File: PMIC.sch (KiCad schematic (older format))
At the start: 71 parts, among them U4 CSD86330Q3D, U5 LMR62014XMF_NOPB, U6 CSD86330Q3D, U8 TPS65086100

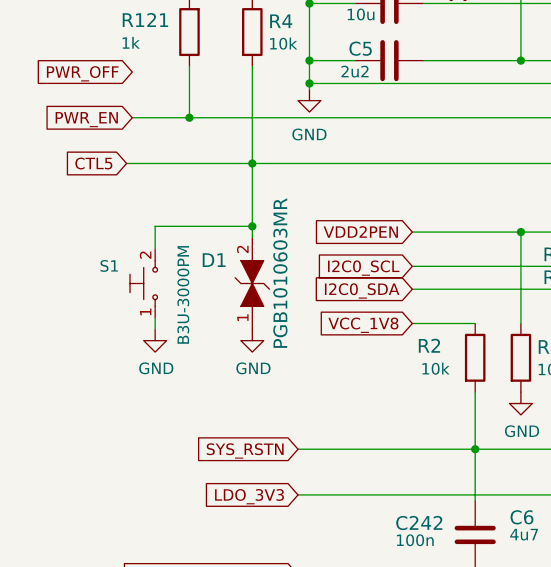
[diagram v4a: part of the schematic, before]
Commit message: Layout: 5v8 dcdc, clocks, SPIFlash, testpoints
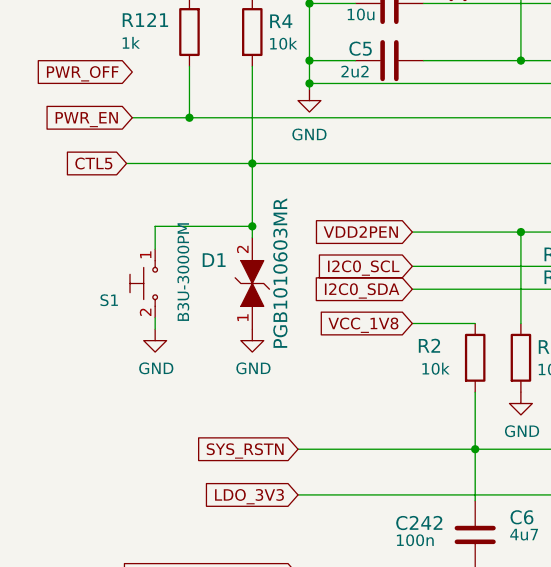
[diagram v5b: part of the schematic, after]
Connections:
- net CTL5: now also S1.1; no longer S1.2
- net GND: now also S1.2; no longer S1.1
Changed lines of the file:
@@
 5V8 boost regulator
-$Comp
-L arvsom:B3U-3000PM S1
-U 1 1 608A76FB
-P 3500 4850
-F 0 "S1" V 3575 5050 50  0000 C CNN
-F 1 "B3U-3000PM" H 3450 4725 50  0000 C CNN
-F 2 "arvsom-footprints:B3U-3000P" H 3700 5050 50  0001 L CNN
-F 3 "http://www.farnell.com/datasheets/2610940.pdf" H 3700 5150 60  0001 L CNN
-F 4 "B3U-3000PM" H 3696 5243 60  0001 L CNN "MPN"
-F 5 "OMRON" H 3700 5322 60  0001 L CNN "Manufacturer"
-	1    3500 4850
-	0    -1   -1   0
-$EndComp
 $Comp
 L arvsom:CSD86330Q3D U4
@@
 	1    0    0    -1
 $EndComp
+$Comp
+L arvsom:B3U-3000PM S1
+U 1 1 608A76FB
+P 3500 4850
+F 0 "S1" V 3575 5050 50  0000 C CNN
+F 1 "B3U-3000PM" H 3450 4725 50  0000 C CNN
+F 2 "arvsom-footprints:B3U-3000P" H 3700 5050 50  0001 L CNN
+F 3 "http://www.farnell.com/datasheets/2610940.pdf" H 3700 5150 60  0001 L CNN
+F 4 "B3U-3000PM" H 3696 5243 60  0001 L CNN "MPN"
+F 5 "OMRON" H 3700 5322 60  0001 L CNN "Manufacturer"
+	1    3500 4850
+	0    -1   1    0
+$EndComp
 $EndSCHEMATC

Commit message: Update libs
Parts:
- R10, R11, R12, R123, R14, R15, R16, R5, R6: footprint antmicro-footprints:0201-res -> arvsom-footprints:0201-res; symbol antmicroResistorsmisc:R_0R_0201 -> arvsom:R_0R_0201
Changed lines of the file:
@@
 	4625 4775 5275 4775
 $Comp
-L antmicroResistorsmisc:R_0R_0201 R5
+L arvsom:R_0R_0201 R5
 U 1 1 60A1EF73
 P 5425 4775
 F 0 "R5" H 5250 4825 60  0000 C CNN
 F 1 "R_0R_0201" H 5425 4625 60  0001 C CNN
-F 2 "antmicro-footprints:0201-res" H 5625 4975 60  0001 L CNN
+F 2 "arvsom-footprints:0201-res" H 5625 4975 60  0001 L CNN
 F 3 "" H 5425 4775 50  0001 C CNN
 F 4 "VISHAY" H 5625 5175 60  0001 L CNN "Manufacturer"
@@
 $EndComp
 $Comp
-L antmicroResistorsmisc:R_0R_0201 R6
+L arvsom:R_0R_0201 R6
 U 1 1 60A26BB5
 P 5425 4875
 F 0 "R6" H 5250 4925 60  0000 C CNN
 F 1 "R_0R_0201" H 5425 4725 60  0001 C CNN
-F 2 "antmicro-footprints:0201-res" H 5625 5075 60  0001 L CNN
+F 2 "arvsom-footprints:0201-res" H 5625 5075 60  0001 L CNN
 F 3 "" H 5425 4875 50  0001 C CNN
 F 4 "VISHAY" H 5625 5275 60  0001 L CNN "Manufacturer"
@@
 $EndComp
 $Comp
-L antmicroResistorsmisc:R_0R_0201 R123
+L arvsom:R_0R_0201 R123
 U 1 1 60A2A03C
 P 5425 5575
 F 0 "R123" H 5375 5675 60  0000 C CNN
 F 1 "R_0R_0201" H 5425 5425 60  0001 C CNN
-F 2 "antmicro-footprints:0201-res" H 5625 5775 60  0001 L CNN
+F 2 "arvsom-footprints:0201-res" H 5625 5775 60  0001 L CNN
 F 3 "" H 5425 5575 50  0001 C CNN
 F 4 "VISHAY" H 5625 5975 60  0001 L CNN "Manufacturer"
@@
 $EndComp
 $Comp
-L antmicroResistorsmisc:R_0R_0201 R10
+L arvsom:R_0R_0201 R10
 U 1 1 60A468A9
 P 8500 3775
 F 0 "R10" H 8275 3825 60  0000 C CNN
 F 1 "R_0R_0201" H 8500 3625 60  0001 C CNN
-F 2 "antmicro-footprints:0201-res" H 8700 3975 60  0001 L CNN
+F 2 "arvsom-footprints:0201-res" H 8700 3975 60  0001 L CNN
 F 3 "" H 8500 3775 50  0001 C CNN
 F 4 "VISHAY" H 8700 4175 60  0001 L CNN "Manufacturer"
@@
 $EndComp
 $Comp
-L antmicroResistorsmisc:R_0R_0201 R11
+L arvsom:R_0R_0201 R11
 U 1 1 60A4B370
 P 8500 3875
 F 0 "R11" H 8275 3925 60  0000 C CNN
 F 1 "R_0R_0201" H 8500 3725 60  0001 C CNN
-F 2 "antmicro-footprints:0201-res" H 8700 4075 60  0001 L CNN
+F 2 "arvsom-footprints:0201-res" H 8700 4075 60  0001 L CNN
 F 3 "" H 8500 3875 50  0001 C CNN
 F 4 "VISHAY" H 8700 4275 60  0001 L CNN "Manufacturer"
@@
 $EndComp
 $Comp
-L antmicroResistorsmisc:R_0R_0201 R12
+L arvsom:R_0R_0201 R12
 U 1 1 60A4C09F
 P 8500 4075
 F 0 "R12" H 8275 4125 60  0000 C CNN
 F 1 "R_0R_0201" H 8500 3925 60  0001 C CNN
-F 2 "antmicro-footprints:0201-res" H 8700 4275 60  0001 L CNN
+F 2 "arvsom-footprints:0201-res" H 8700 4275 60  0001 L CNN
 F 3 "" H 8500 4075 50  0001 C CNN
 F 4 "VISHAY" H 8700 4475 60  0001 L CNN "Manufacturer"
@@
 $EndComp
 $Comp
-L antmicroResistorsmisc:R_0R_0201 R14
+L arvsom:R_0R_0201 R14
 U 1 1 60A523FE
 P 8500 5375
 F 0 "R14" H 8275 5425 60  0000 C CNN
 F 1 "R_0R_0201" H 8500 5225 60  0001 C CNN
-F 2 "antmicro-footprints:0201-res" H 8700 5575 60  0001 L CNN
+F 2 "arvsom-footprints:0201-res" H 8700 5575 60  0001 L CNN
 F 3 "" H 8500 5375 50  0001 C CNN
 F 4 "VISHAY" H 8700 5775 60  0001 L CNN "Manufacturer"
@@
 $EndComp
 $Comp
-L antmicroResistorsmisc:R_0R_0201 R15
+L arvsom:R_0R_0201 R15
 U 1 1 60A56682
 P 8500 5475
 F 0 "R15" H 8275 5525 60  0000 C CNN
 F 1 "R_0R_0201" H 8500 5325 60  0001 C CNN
-F 2 "antmicro-footprints:0201-res" H 8700 5675 60  0001 L CNN
+F 2 "arvsom-footprints:0201-res" H 8700 5675 60  0001 L CNN
 F 3 "" H 8500 5475 50  0001 C CNN
 F 4 "VISHAY" H 8700 5875 60  0001 L CNN "Manufacturer"
@@
 $EndComp
 $Comp
-L antmicroResistorsmisc:R_0R_0201 R16
+L arvsom:R_0R_0201 R16
 U 1 1 60A57367
 P 8500 5675
 F 0 "R16" H 8275 5725 60  0000 C CNN
 F 1 "R_0R_0201" H 8500 5525 60  0001 C CNN
-F 2 "antmicro-footprints:0201-res" H 8700 5875 60  0001 L CNN
+F 2 "arvsom-footprints:0201-res" H 8700 5875 60  0001 L CNN
 F 3 "" H 8500 5675 50  0001 C CNN
 F 4 "VISHAY" H 8700 6075 60  0001 L CNN "Manufacturer"

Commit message: Update lib attributes
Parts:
- U2: renamed from U8; MPN (none) -> TPS65086100; Manufacturer (none) -> Texas Instruments
- U5: Manufacturer (none) -> Texas Instruments
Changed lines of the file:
@@
 $EndComp
 $Comp
-L arvsom:TPS65086100 U8
+L arvsom:TPS65086100 U2
 U 1 1 606F10CB
 P 6225 2925
-F 0 "U8" H 7125 3090 50  0000 C CNN
+F 0 "U2" H 7125 3090 50  0000 C CNN
 F 1 "TPS65086100" H 7125 2999 50  0000 C CNN
 F 2 "arvsom-footprints:S-PVQFN-N64" H 8025 2975 50  0001 C CNN
 F 3 "" H 6225 2925 50  0001 C CNN
+F 4 "TPS65086100" H 6225 2925 50  0001 C CNN "MPN"
+F 5 "Texas Instruments" H 6225 2925 50  0001 C CNN "Manufacturer"
 	1    6225 2925
 	1    0    0    -1
@@
 F 3 "" H 7000 9775 50  0001 L BNN
 F 4 "LMR62014XMF" H 7000 10253 50  0001 C CNN "MPN"
+F 5 "Texas Instruments" H 7000 9775 50  0001 C CNN "Manufacturer"
 	1    7000 9775
 	1    0    0    -1
